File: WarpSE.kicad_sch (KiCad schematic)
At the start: 9 parts

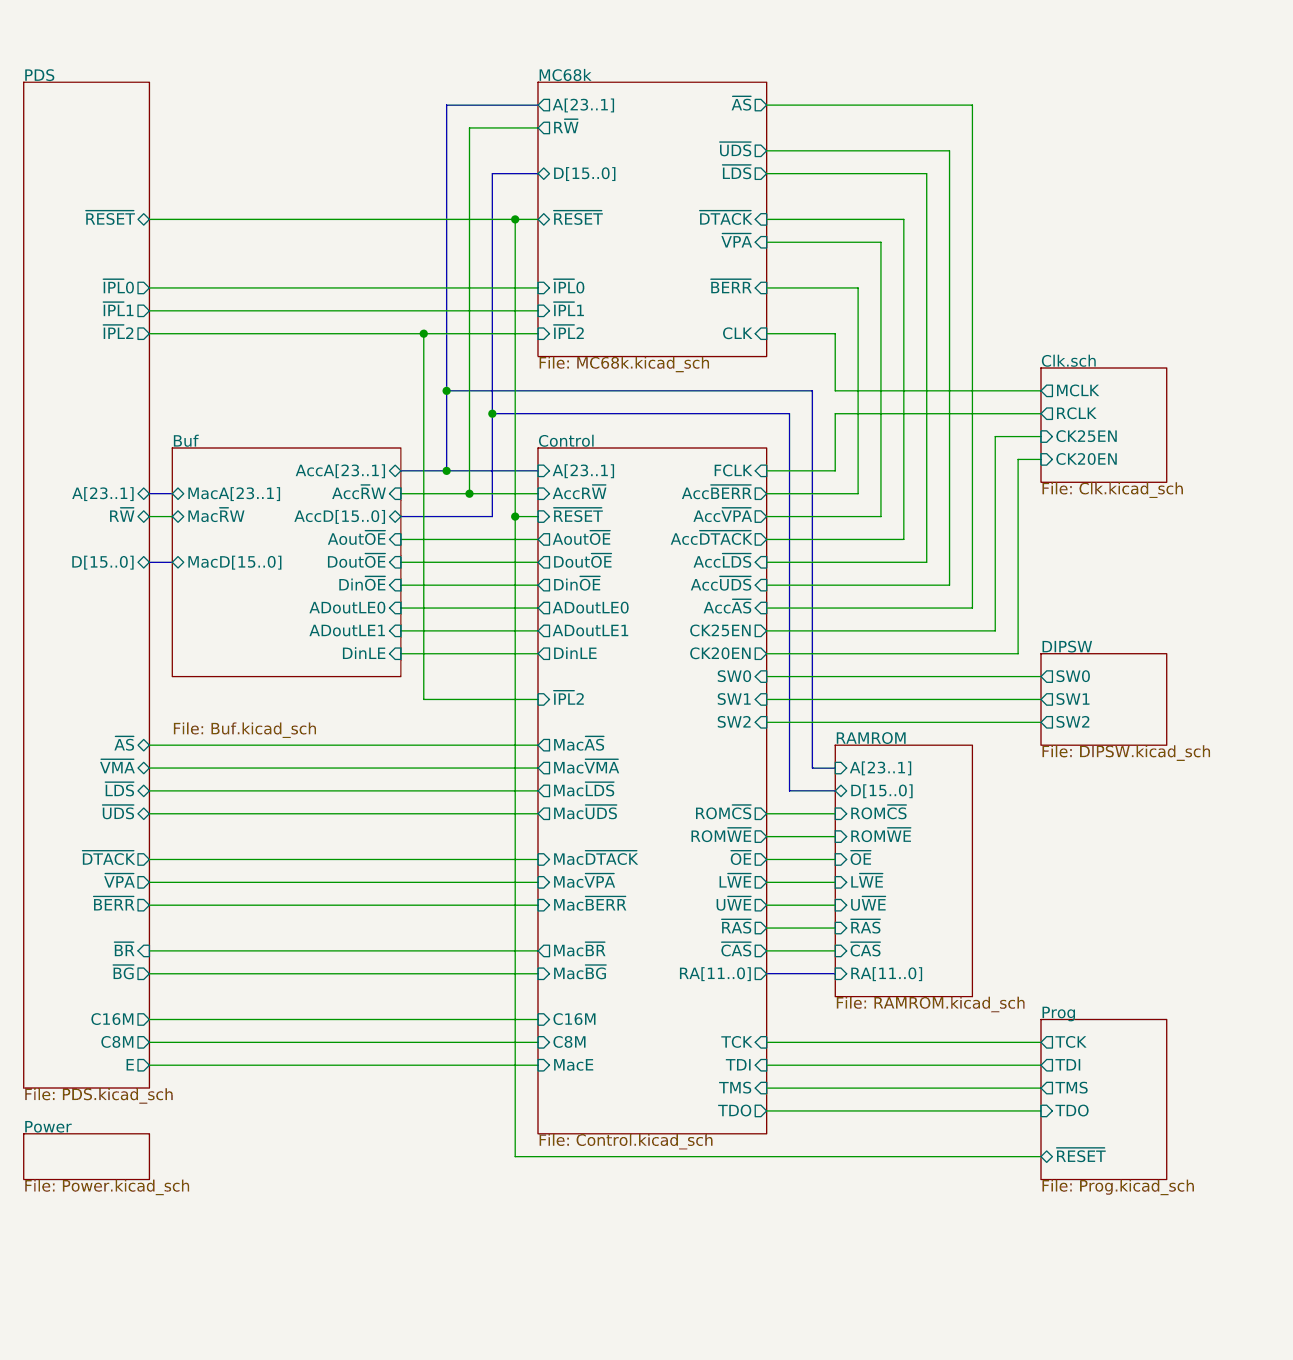
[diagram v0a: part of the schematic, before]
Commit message: working on SDRAM
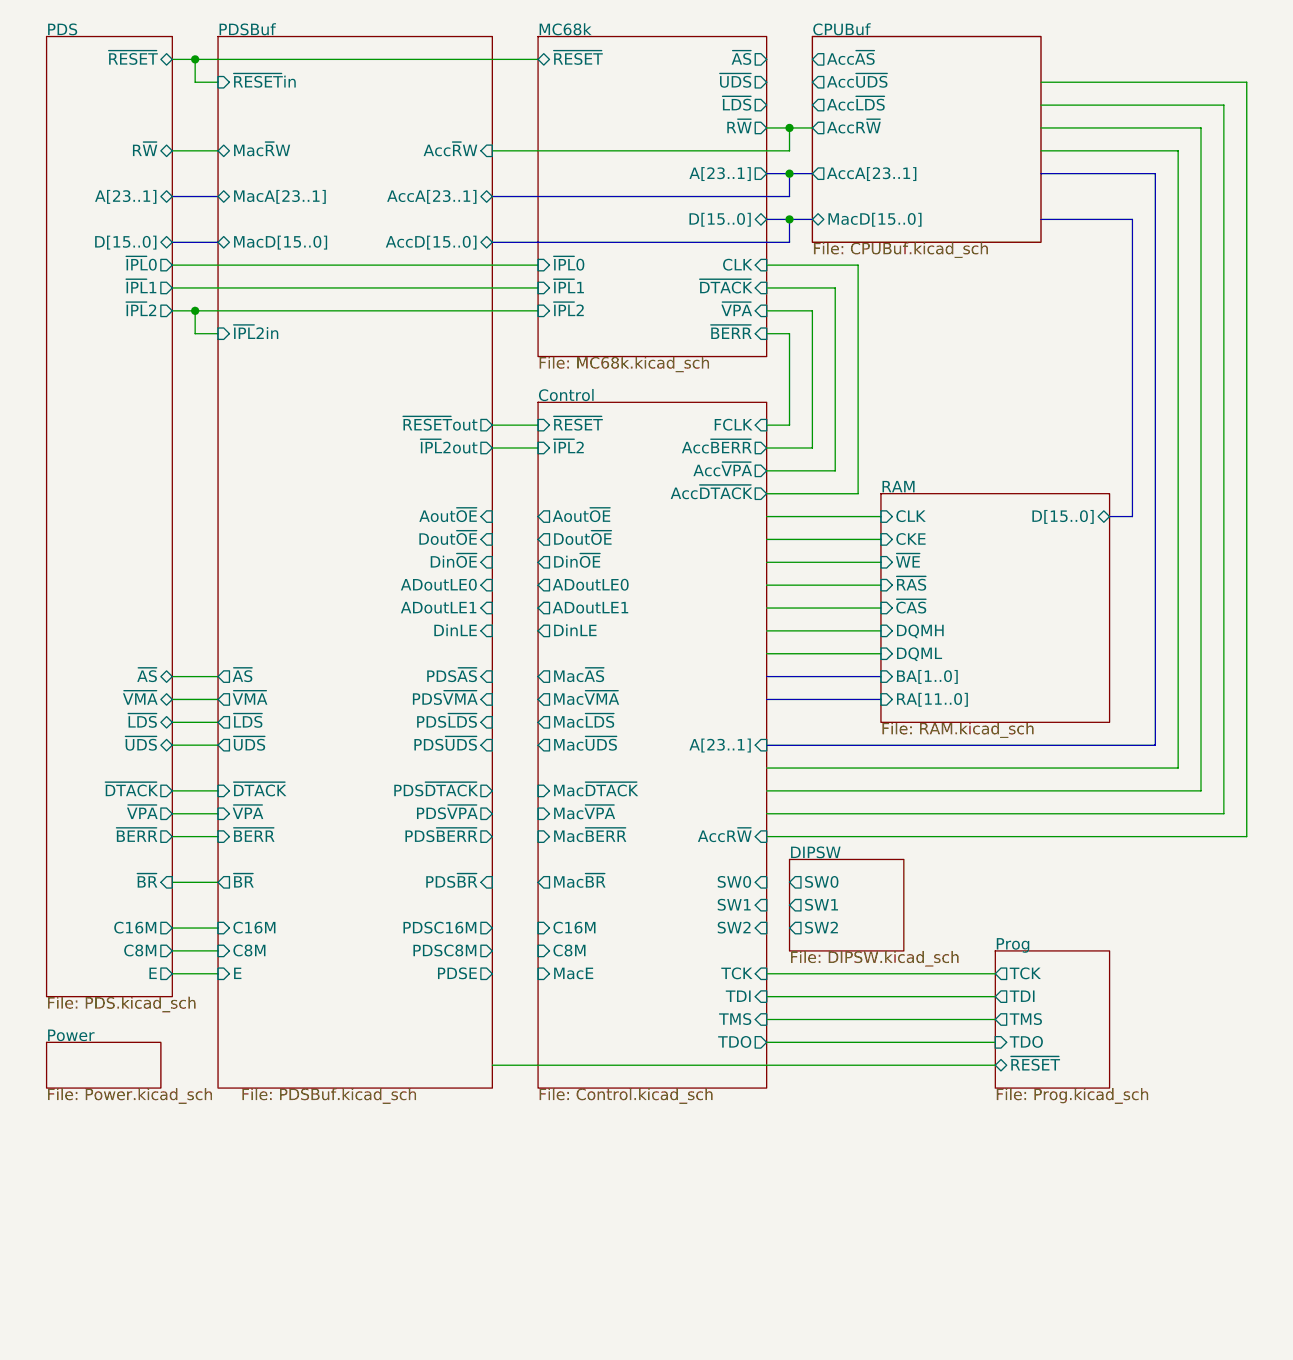
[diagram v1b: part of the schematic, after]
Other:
- sheet Buf renamed PDSBuf
- sheet RAMROM renamed RAM
- removed sheet Clk.sch
- added sheet CPUBuf (CPUBuf.kicad_sch)
- sheet Control ports: added none; removed Acc~{AS}, Acc~{LDS}, Acc~{UDS}, CK20EN, CK25EN, L~{WE}, Mac~{BG}, RA[11..0], ROM~{CS}, ROM~{WE}, U~{WE}, ~{CAS}, ~{OE}, ~{RAS}
- sheet PDS ports: added none; removed ~{BG}
- sheet PDSBuf: file Buf.kicad_sch -> PDSBuf.kicad_sch
- sheet PDSBuf ports: added C16M, C8M, E, PDSC16M, PDSC8M, PDSE, PDS~{AS}, PDS~{BERR}, PDS~{BR}, PDS~{DTACK}, PDS~{LDS}, PDS~{UDS}, PDS~{VMA}, PDS~{VPA}, ~{AS}, ~{BERR}, ~{BR}, ~{DTACK}, ~{IPL}2in, ~{IPL}2out, ~{LDS}, ~{RESET}in, ~{RESET}out, ~{UDS}, ~{VMA}, ~{VPA}; removed none
- sheet RAM: file RAMROM.kicad_sch -> RAM.kicad_sch
- sheet RAM ports: added BA[1..0], CKE, CLK, DQMH, DQML, ~{WE}; removed A[23..1], L~{WE}, ROM~{CS}, ROM~{WE}, U~{WE}, ~{OE}

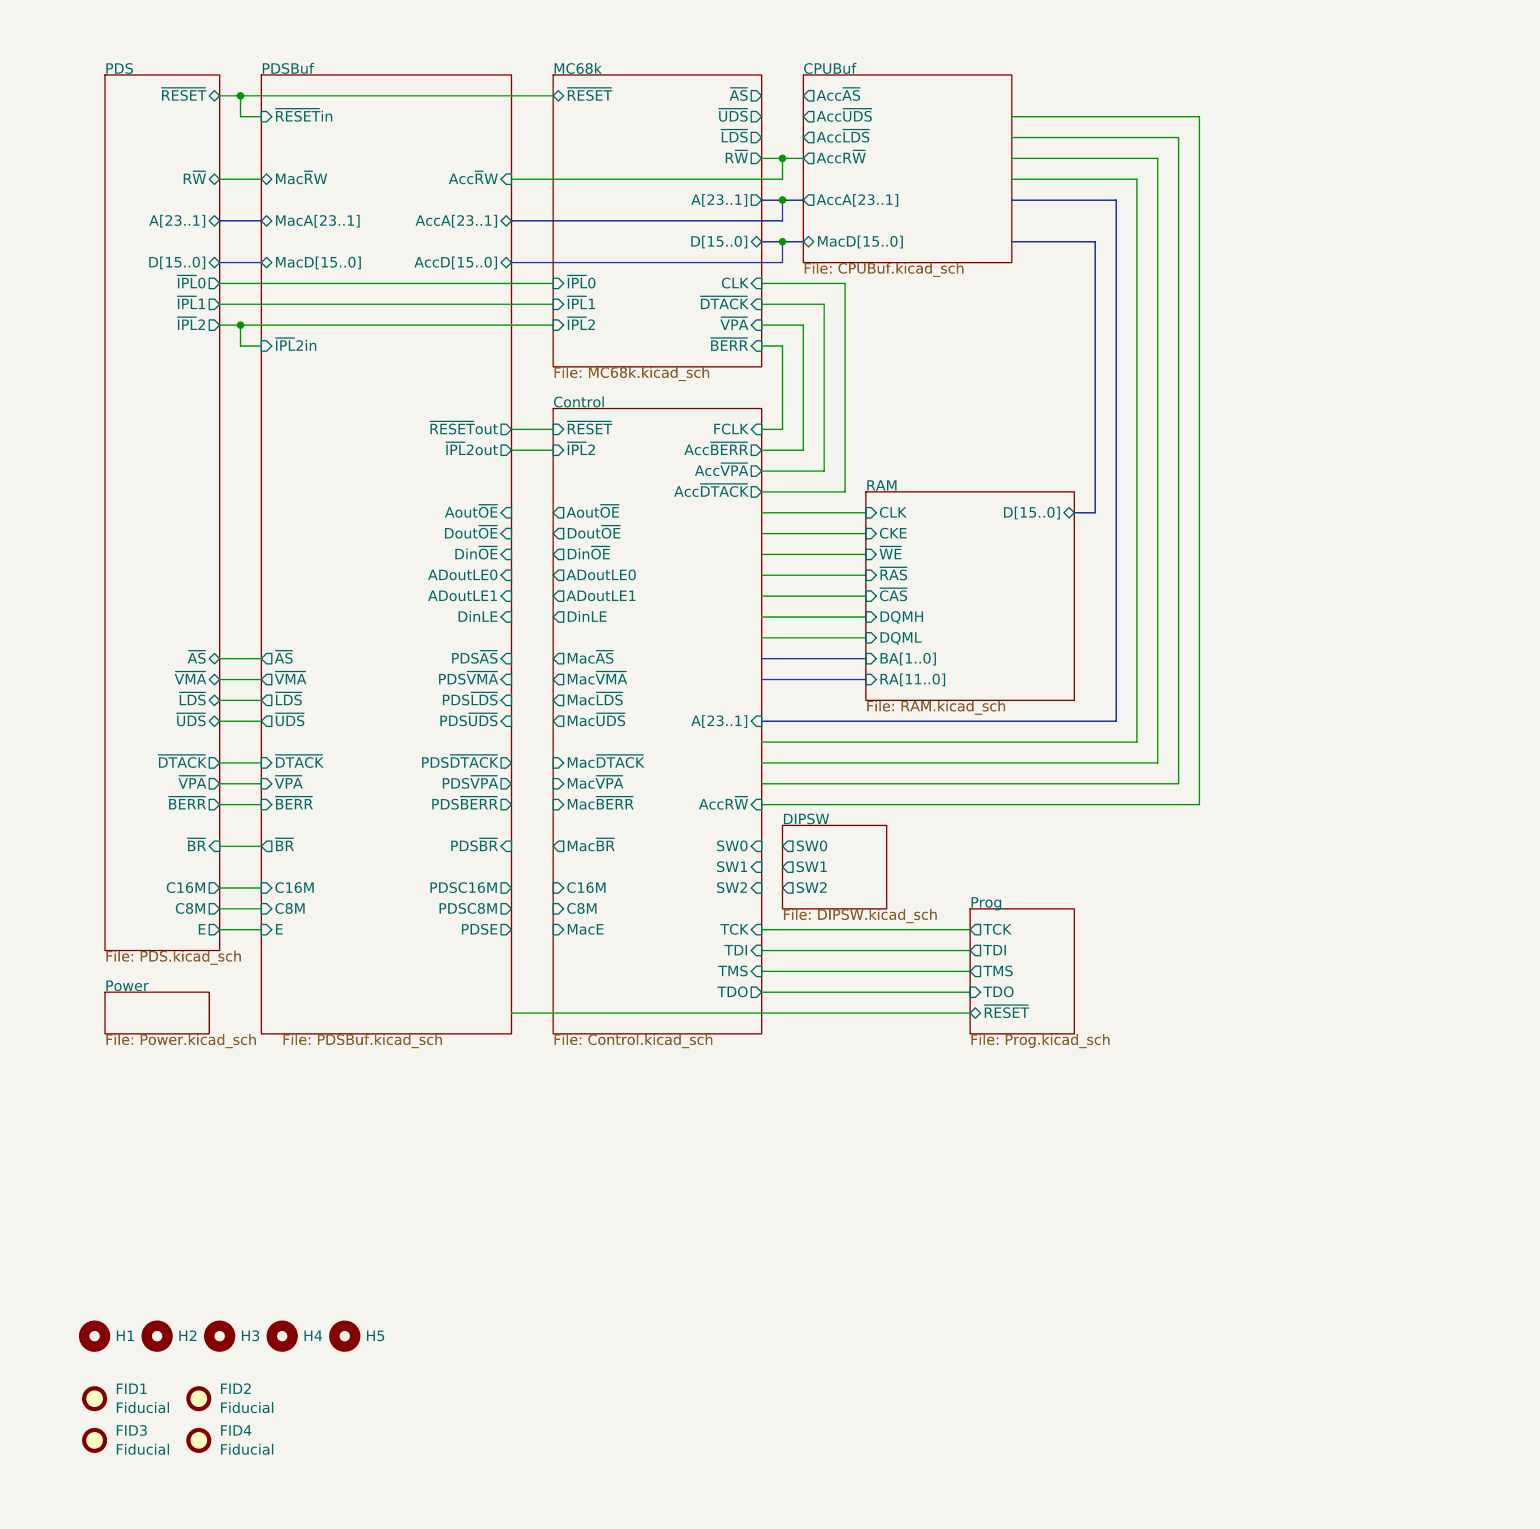
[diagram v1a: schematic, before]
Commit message: Switch to '030
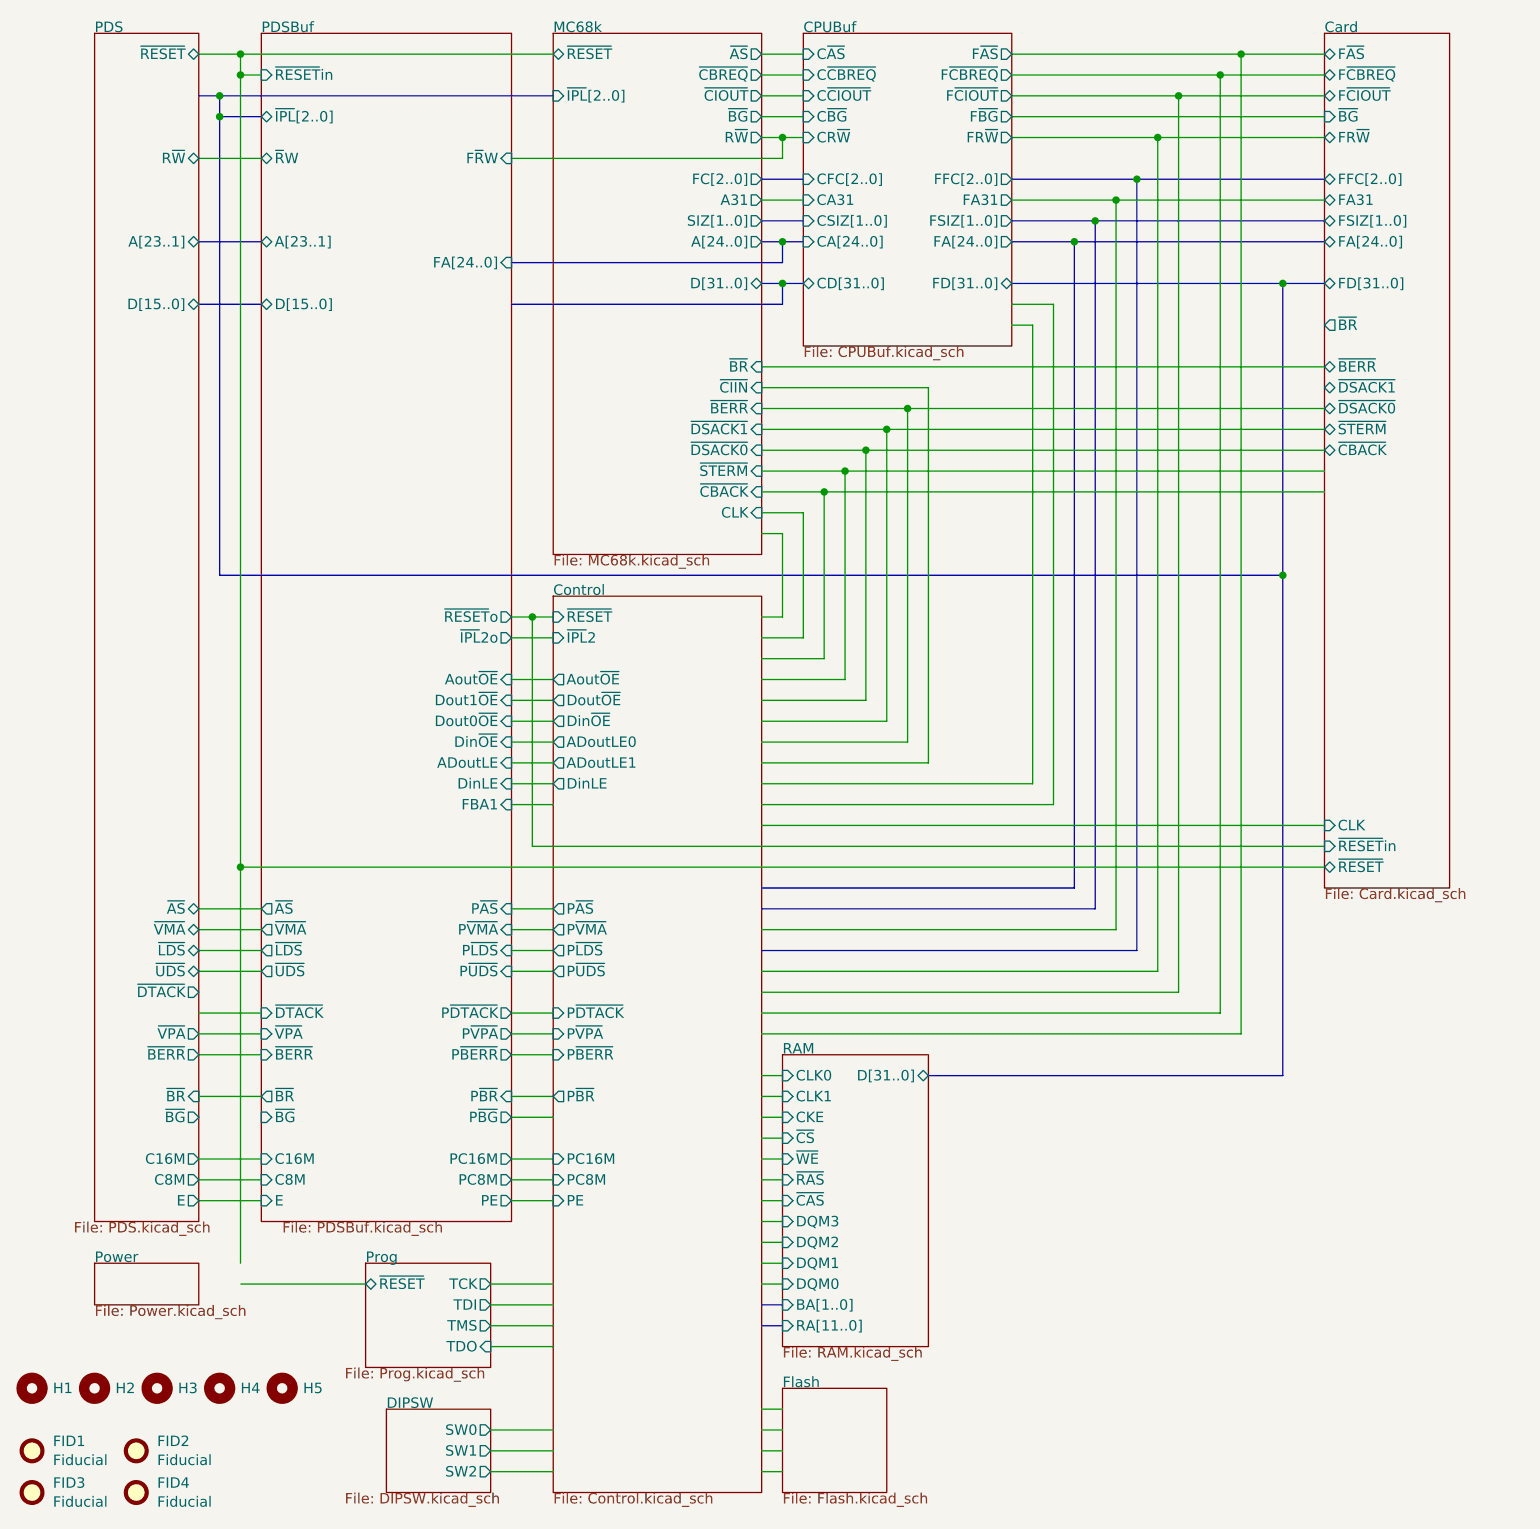
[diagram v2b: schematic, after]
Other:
- added sheet Card (Card.kicad_sch)
- added sheet Flash (Flash.kicad_sch)
- sheet CPUBuf ports: added CA31, CA[24..0], CD[31..0], CFC[2..0], CR~{W}, CSIZ[1..0], C~{AS}, C~{BG}, C~{CBREQ}, C~{CIOUT}, FA31, FA[24..0], FD[31..0], FFC[2..0], FR~{W}, FSIZ[1..0], F~{AS}, F~{BG}, F~{CBREQ}, F~{CIOUT}; removed AccA[23..1], AccR~{W}, Acc~{AS}, Acc~{LDS}, Acc~{UDS}, MacD[15..0]
- sheet Control ports: added PC16M, PC8M, PE, P~{AS}, P~{BERR}, P~{BR}, P~{DTACK}, P~{LDS}, P~{UDS}, P~{VMA}, P~{VPA}; removed A[23..1], AccR~{W}, Acc~{BERR}, Acc~{DTACK}, Acc~{VPA}, C16M, C8M, FCLK, MacE, Mac~{AS}, Mac~{BERR}, Mac~{BR}, Mac~{DTACK}, Mac~{LDS}, Mac~{UDS}, Mac~{VMA}, Mac~{VPA}, SW0, SW1, SW2, TCK, TDI, TDO, TMS
- sheet MC68k ports: added A31, A[24..0], D[31..0], FC[2..0], SIZ[1..0], ~{BG}, ~{BR}, ~{CBACK}, ~{CBREQ}, ~{CIIN}, ~{CIOUT}, ~{DSACK0}, ~{DSACK1}, ~{IPL}[2..0], ~{STERM}; removed A[23..1], D[15..0], ~{DTACK}, ~{IPL}0, ~{IPL}1, ~{IPL}2, ~{LDS}, ~{UDS}, ~{VPA}
- sheet PDS ports: added ~{BG}; removed ~{IPL}0, ~{IPL}1, ~{IPL}2
- sheet PDSBuf ports: added ADoutLE, A[23..1], D[15..0], Dout0~{OE}, Dout1~{OE}, FA[24..0], FBA1, F~{R}W, PC16M, PC8M, PE, P~{AS}, P~{BERR}, P~{BG}, P~{BR}, P~{DTACK}, P~{LDS}, P~{UDS}, P~{VMA}, P~{VPA}, ~{BG}, ~{IPL}2o, ~{IPL}[2..0], ~{RESET}o, ~{R}W; removed ADoutLE0, ADoutLE1, AccA[23..1], AccD[15..0], Acc~{R}W, Dout~{OE}, MacA[23..1], MacD[15..0], Mac~{R}W, PDSC16M, PDSC8M, PDSE, PDS~{AS}, PDS~{BERR}, PDS~{BR}, PDS~{DTACK}, PDS~{LDS}, PDS~{UDS}, PDS~{VMA}, PDS~{VPA}, ~{IPL}2in, ~{IPL}2out, ~{RESET}out
- sheet RAM ports: added CLK0, CLK1, DQM0, DQM1, DQM2, DQM3, D[31..0], ~{CS}; removed CLK, DQMH, DQML, D[15..0]
- moved on the sheet: FID1, FID2, FID3, FID4, H1, H2, H3, H4, H5

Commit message: idk
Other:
- removed sheet CPUBuf
- removed sheet Card
- removed sheet MC68k
- sheet PDSBuf ports: added BA[23..1], B~{R}W; removed FA[24..0], F~{R}W

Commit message: more
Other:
- sheet Control ports: added AoutLE; removed ADoutLE0, ADoutLE1, DinLE, ~{RESET}
- sheet PDSBuf ports: added AHoutLE, ALoutLE, AoutLE, BC16M, BC8M, BE, B~{BERR}, B~{BG}, B~{DTACK}, B~{IPL}[2..0], B~{RESET}, B~{VPA}, DDIR, D~{OE}, FA[23..1], O~{AS}, O~{BR}, O~{LDS}, O~{R}W, O~{UDS}, O~{VMA}, ~{RESETOE}, ~{RESET}; removed ADoutLE, DinLE, Din~{OE}, Dout0~{OE}, Dout1~{OE}, FBA1, ~{IPL}2o
- sheet RAM ports: added A[23..1], CLK, DQMH, DQML, D[15..0]; removed BA[1..0], CLK0, CLK1, DQM0, DQM1, DQM2, DQM3, D[31..0], RA[11..0], ~{CS}

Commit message: more
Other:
- removed sheet DIPSW
- sheet Control ports: added AHLE, ALLE, A~{OE}, BD[15..0], B~{RESET}, C16M, C8M, CKE, CLK, DDIR, DQMH, DQML, D~{OE}, E, FA[23..1], OR~{W}, O~{RESET}, RD[15..0], TCK, TDI, TDO, TMS, ~{AS}, ~{BERR}, ~{BG}, ~{BR}, ~{CAS}, ~{DTACK}, ~{IPL}[2..0], ~{LDS}, ~{RAS}, ~{UDS}, ~{VMA}, ~{VPA}, ~{WE}; removed AoutLE, Aout~{OE}, Din~{OE}, Dout~{OE}, PC16M, PC8M, PE, P~{AS}, P~{BERR}, P~{BR}, P~{DTACK}, P~{LDS}, P~{UDS}, P~{VMA}, P~{VPA}, ~{IPL}2
- sheet PDS ports: added ~{IPL}[2..0]; removed none
- sheet PDSBuf ports: added AHLE, ALLE, A~{OE}, BD[15..0]; removed AHoutLE, ALoutLE, AoutLE, Aout~{OE}, BA[23..1], B~{R}W, PC16M, PC8M, PE, P~{AS}, P~{BERR}, P~{BG}, P~{BR}, P~{DTACK}, P~{LDS}, P~{UDS}, P~{VMA}, P~{VPA}, ~{RESETOE}, ~{RESET}in, ~{RESET}o
